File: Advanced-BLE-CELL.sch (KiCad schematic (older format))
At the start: 18 parts, among them J3 40HAT, J6 CONN_02X02, J9 CONN_01X02, Q1 DMG2305UX, Q2 DMMT5401, U2 CAT24C32

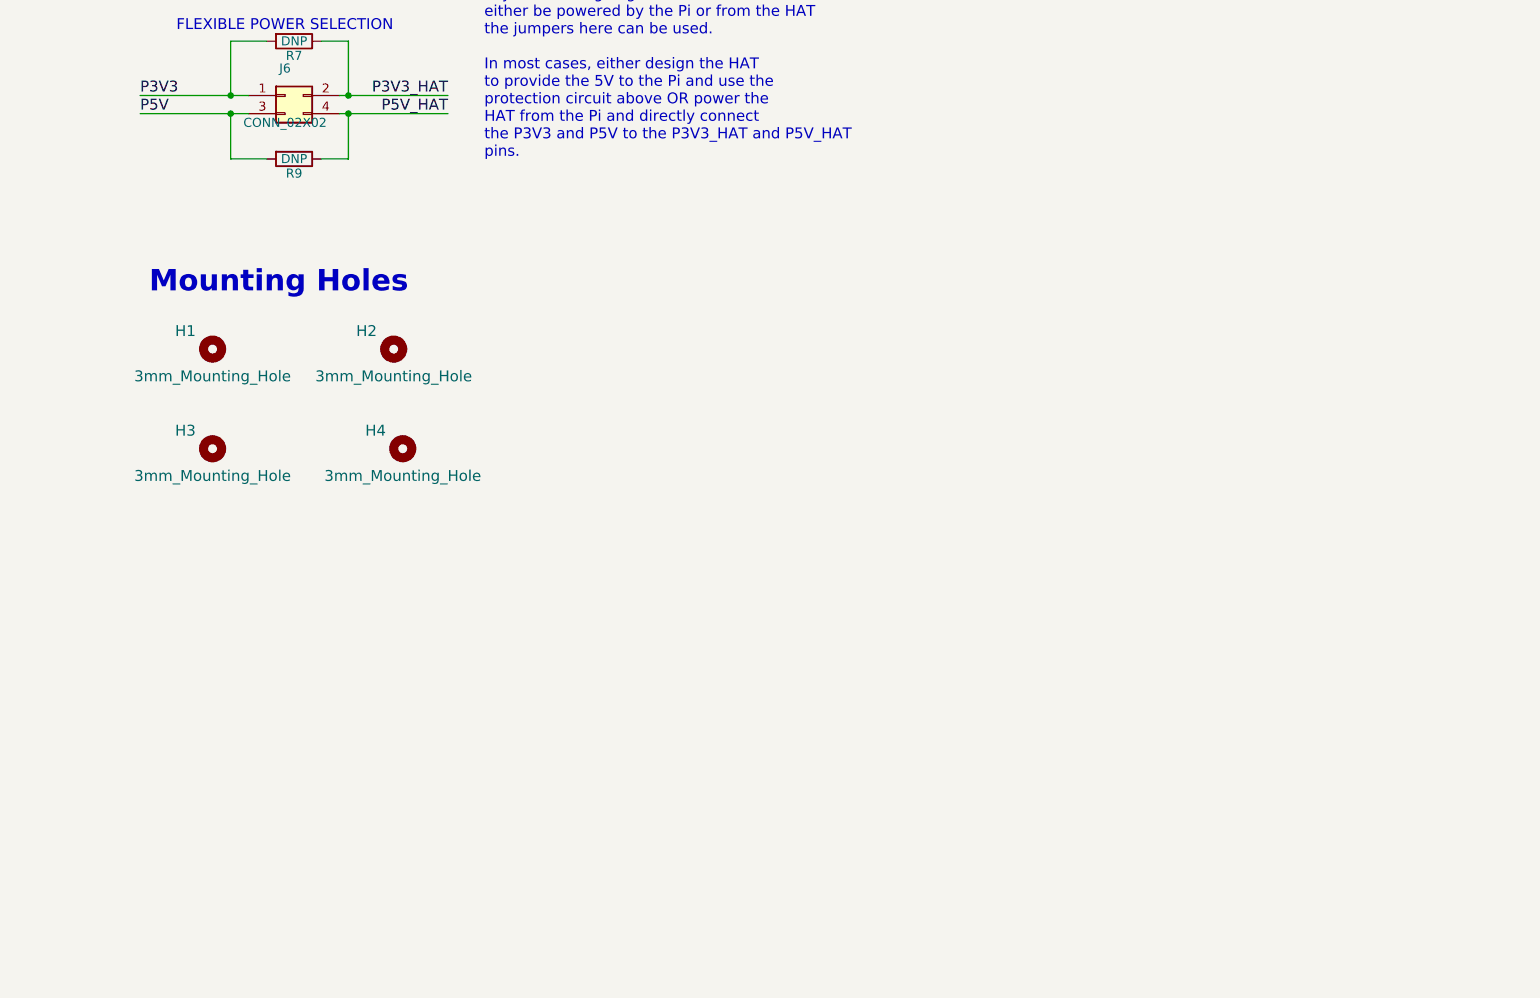
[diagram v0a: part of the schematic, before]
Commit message: Added Symbols & footprints for BG95, NRF52840 and 4881 breakout mounting holes
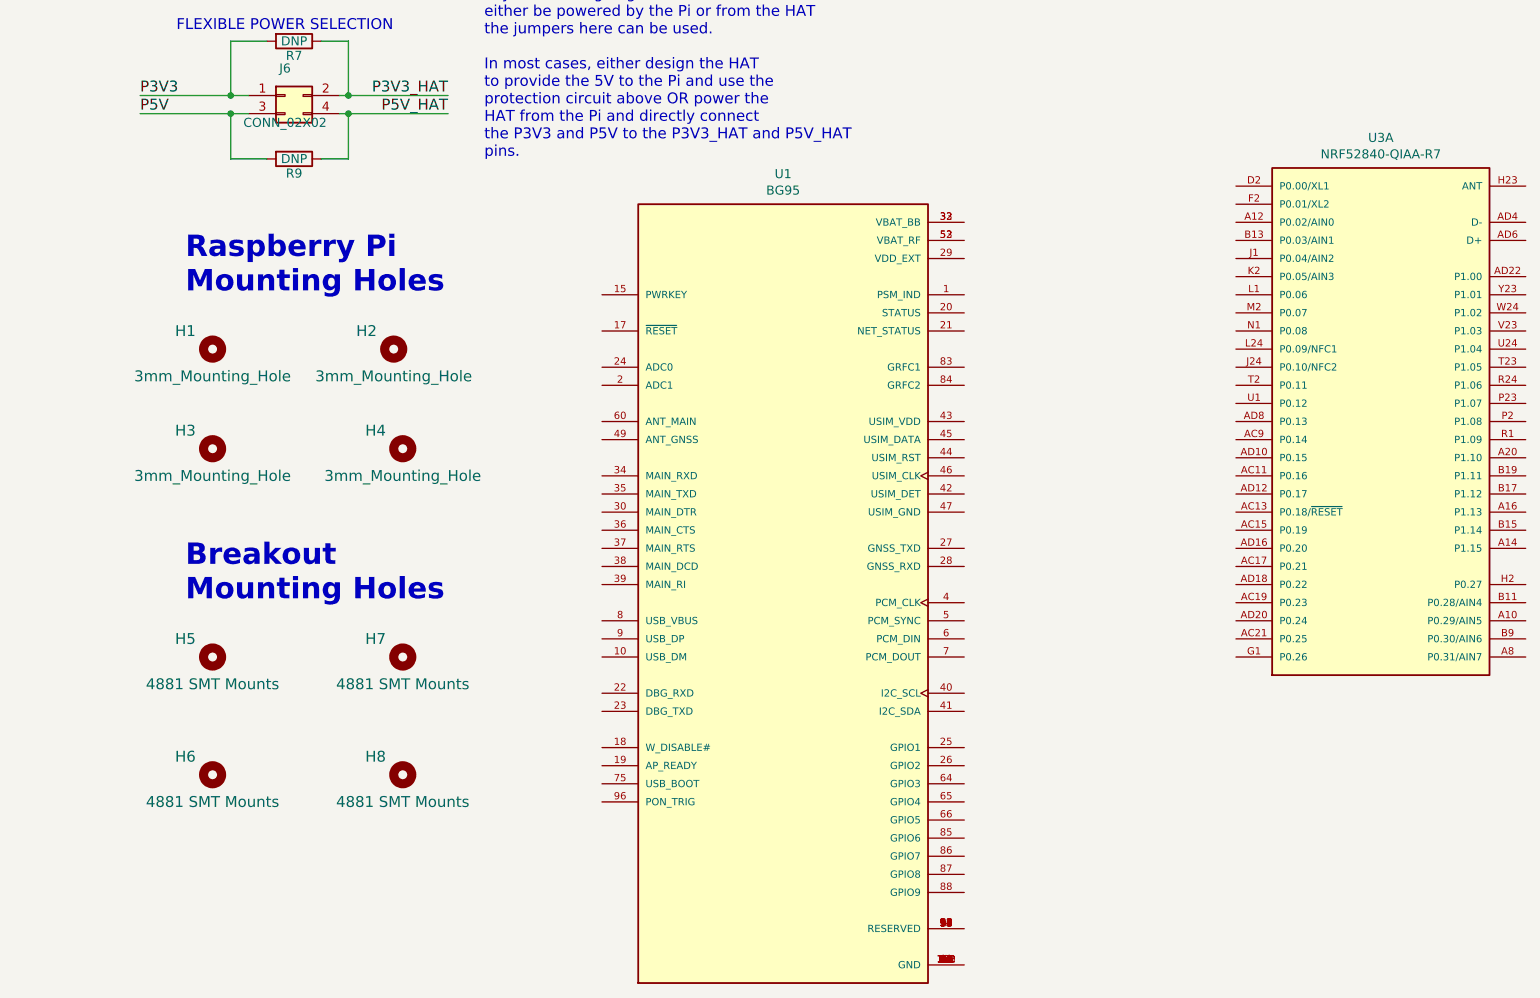
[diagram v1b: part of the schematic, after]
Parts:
- added H5, H6, H7, H8: 4881 SMT Mounts, project_footprints:4881, symbol Mechanical:MountingHole
- added U1: BG95, XCVR_BG95, symbol BG95:BG95
- added U3: NRF52840-QIAA-R7, NORDIC_NRF52840-QIAA-R7, symbol NRF52840-QIAA-R7:NRF52840-QIAA-R7
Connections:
- new net: U1.100 (GND), U1.101 (GND), U1.102 (GND), U1.3 (GND), U1.31 (GND), U1.48 (GND), U1.50 (GND), U1.54 (GND), U1.55 (GND), U1.58 (GND), U1.59 (GND), U1.61 (GND), U1.62 (GND), U1.67 (GND), U1.68 (GND), U1.69 (GND), U1.70 (GND), U1.71 (GND), U1.72 (GND), U1.73 (GND), U1.74 (GND), U1.79 (GND), U1.80 (GND), U1.81 (GND), U1.82 (GND), U1.89 (GND), U1.90 (GND), U1.91 (GND)
- new net: U1.11 (RESERVED), U1.12 (RESERVED), U1.13 (RESERVED), U1.14 (RESERVED), U1.16 (RESERVED), U1.51 (RESERVED), U1.56 (RESERVED), U1.57 (RESERVED), U1.63 (RESERVED), U1.76 (RESERVED), U1.77 (RESERVED), U1.78 (RESERVED), U1.92 (RESERVED), U1.93 (RESERVED), U1.94 (RESERVED), U1.95 (RESERVED), U1.97 (RESERVED), U1.98 (RESERVED), U1.99 (RESERVED)
- new net: U1.32 (VBAT_BB), U1.33 (VBAT_BB)
- new net: U1.52 (VBAT_RF), U1.53 (VBAT_RF)
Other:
- note added: "Breakout\nMounting Holes"
- note added: "Raspberry Pi\nMounting Holes"
- note removed: "Mounting Holes"
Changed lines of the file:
@@
 EESchema Schematic File Version 4
-LIBS:raspberrypi_hat-cache
-EELAYER 29 0
+EELAYER 30 0
 EELAYER END
 $Descr A3 16535 11693
@@
 Text Notes 2000 4800 0    118  ~ 24
 HAT EEPROM
-Text Notes 5300 5700 0    118  ~ 24
-Mounting Holes
+Text Notes 5500 5700 0    118  ~ 24
+Raspberry Pi\nMounting Holes
 Text Notes 1650 2000 0    118  ~ 24
 40-Pin HAT Connector
@@
 Wire Wire Line
 	1050 6100 1150 6100
+$Comp
+L BG95:BG95 U1
+U 1 1 60AAF1CA
+P 8800 7300
+F 0 "U1" H 8800 9567 50  0000 C CNN
+F 1 "BG95" H 8800 9476 50  0000 C CNN
+F 2 "XCVR_BG95" H 8800 7300 50  0001 L BNN
+F 3 "" H 8800 7300 50  0001 L BNN
+F 4 "1.1" H 8800 7300 50  0001 L BNN "PARTREV"
+F 5 "2.4 mm" H 8800 7300 50  0001 L BNN "MAXIMUM_PACKAGE_HEIGHT"
+F 6 "Manufacturer Recommendations" H 8800 7300 50  0001 L BNN "STANDARD"
+F 7 "Quectel" H 8800 7300 50  0001 L BNN "MANUFACTURER"
+	1    8800 7300
+	1    0    0    -1
+$EndComp
+$Comp
+L Mechanical:MountingHole H5
+U 1 1 60AB5B92
+P 5650 7700
+F 0 "H5" H 5500 7800 60  0000 C CNN
+F 1 "4881 SMT Mounts" H 5650 7550 60  0000 C CNN
+F 2 "project_footprints:4881" H 5550 7700 60  0001 C CNN
+F 3 "" H 5550 7700 60  0001 C CNN
+	1    5650 7700
+	1    0    0    -1
+$EndComp
+Text Notes 5500 7400 0    118  ~ 24
+Breakout\nMounting Holes
+$Comp
+L Mechanical:MountingHole H7
+U 1 1 60AB87F6
+P 6700 7700
+F 0 "H7" H 6550 7800 60  0000 C CNN
+F 1 "4881 SMT Mounts" H 6700 7550 60  0000 C CNN
+F 2 "project_footprints:4881" H 6600 7700 60  0001 C CNN
+F 3 "" H 6600 7700 60  0001 C CNN
+	1    6700 7700
+	1    0    0    -1
+$EndComp
+$Comp
+L Mechanical:MountingHole H8
+U 1 1 60ABAB16
+P 6700 8350
+F 0 "H8" H 6550 8450 60  0000 C CNN
+F 1 "4881 SMT Mounts" H 6700 8200 60  0000 C CNN
+F 2 "project_footprints:4881" H 6600 8350 60  0001 C CNN
+F 3 "" H 6600 8350 60  0001 C CNN
+	1    6700 8350
+	1    0    0    -1
+$EndComp
+$Comp
+L Mechanical:MountingHole H6
+U 1 1 60ABCE73
+P 5650 8350
+F 0 "H6" H 5500 8450 60  0000 C CNN
+F 1 "4881 SMT Mounts" H 5650 8200 60  0000 C CNN
+F 2 "project_footprints:4881" H 5550 8350 60  0001 C CNN
+F 3 "" H 5550 8350 60  0001 C CNN
+	1    5650 8350
+	1    0    0    -1
+$EndComp
+$Comp
+L NRF52840-QIAA-R7:NRF52840-QIAA-R7 U3
+U 1 1 60ACBB4C
+P 12100 6400
+F 0 "U3" H 12100 7967 50  0000 C CNN
+F 1 "NRF52840-QIAA-R7" H 12100 7876 50  0000 C CNN
+F 2 "NORDIC_NRF52840-QIAA-R7" H 12100 6400 50  0001 L BNN
+F 3 "" H 12100 6400 50  0001 L BNN
+F 4 "NORDIC SEMICONDUCTOR" H 12100 6400 50  0001 L BNN "MF"
+	1    12100 6400
+	1    0    0    -1
+$EndComp
 $EndSCHEMATC
